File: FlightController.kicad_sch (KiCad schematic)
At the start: 0 parts

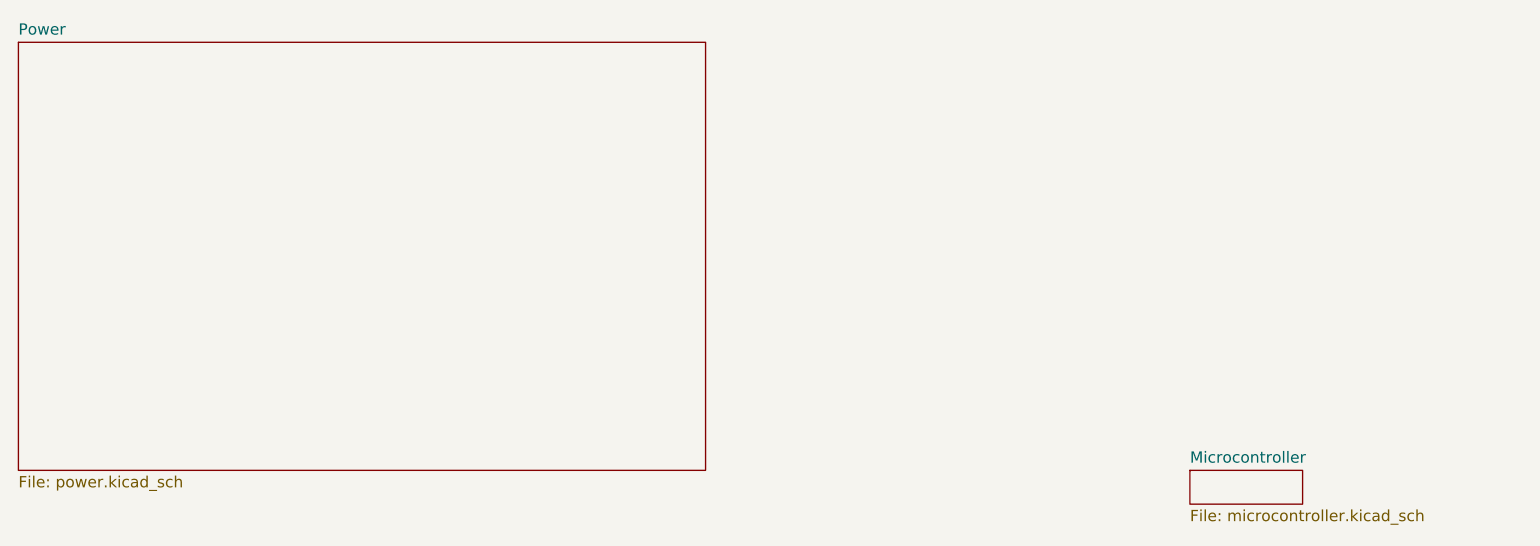
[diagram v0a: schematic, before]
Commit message: Added the power and gnd connections, decoupling capacitors and the reset circuit. Need to finish clock/oscillator, boot configuration, and programming interface schematics.
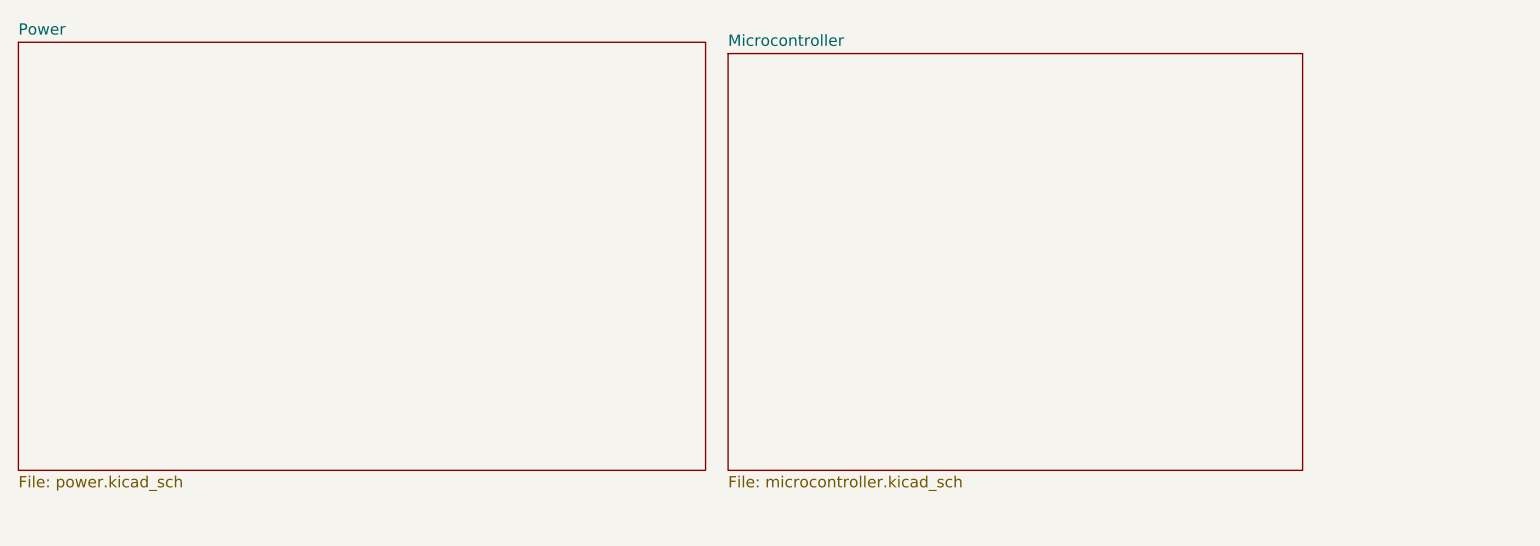
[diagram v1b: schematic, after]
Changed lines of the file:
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@@
 	(paper "A4")
 	(sheet
-		(at 146.05 63.5)
-		(size 12.7 3.81)
+		(at 93.98 16.51)
+		(size 64.77 46.99)
 		(exclude_from_sim no)
 		(in_bom yes)
@@
 		)
 		(property "Sheetname" "Microcontroller"
-			(at 146.05 62.7884 0)
+			(at 93.98 15.7984 0)
 			(show_name no)
 			(do_not_autoplace no)
@@
 		)
 		(property "Sheetfile" "microcontroller.kicad_sch"
-			(at 146.05 67.8946 0)
+			(at 93.98 64.0846 0)
 			(show_name no)
 			(do_not_autoplace no)
